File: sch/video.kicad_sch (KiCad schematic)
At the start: 4 parts

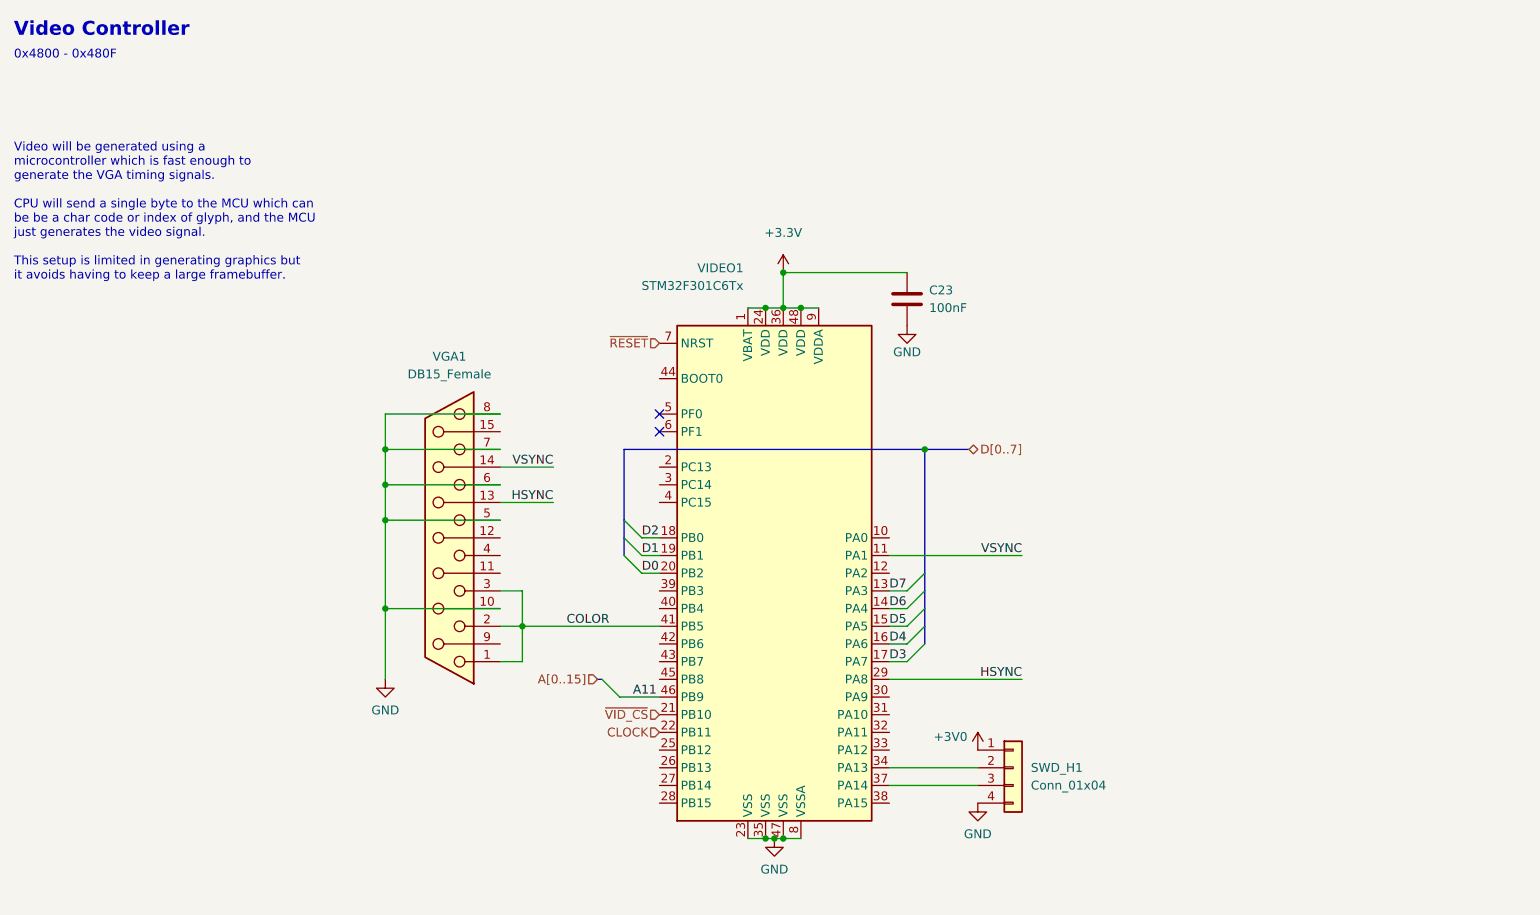
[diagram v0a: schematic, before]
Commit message: fix peripherals, add SPI
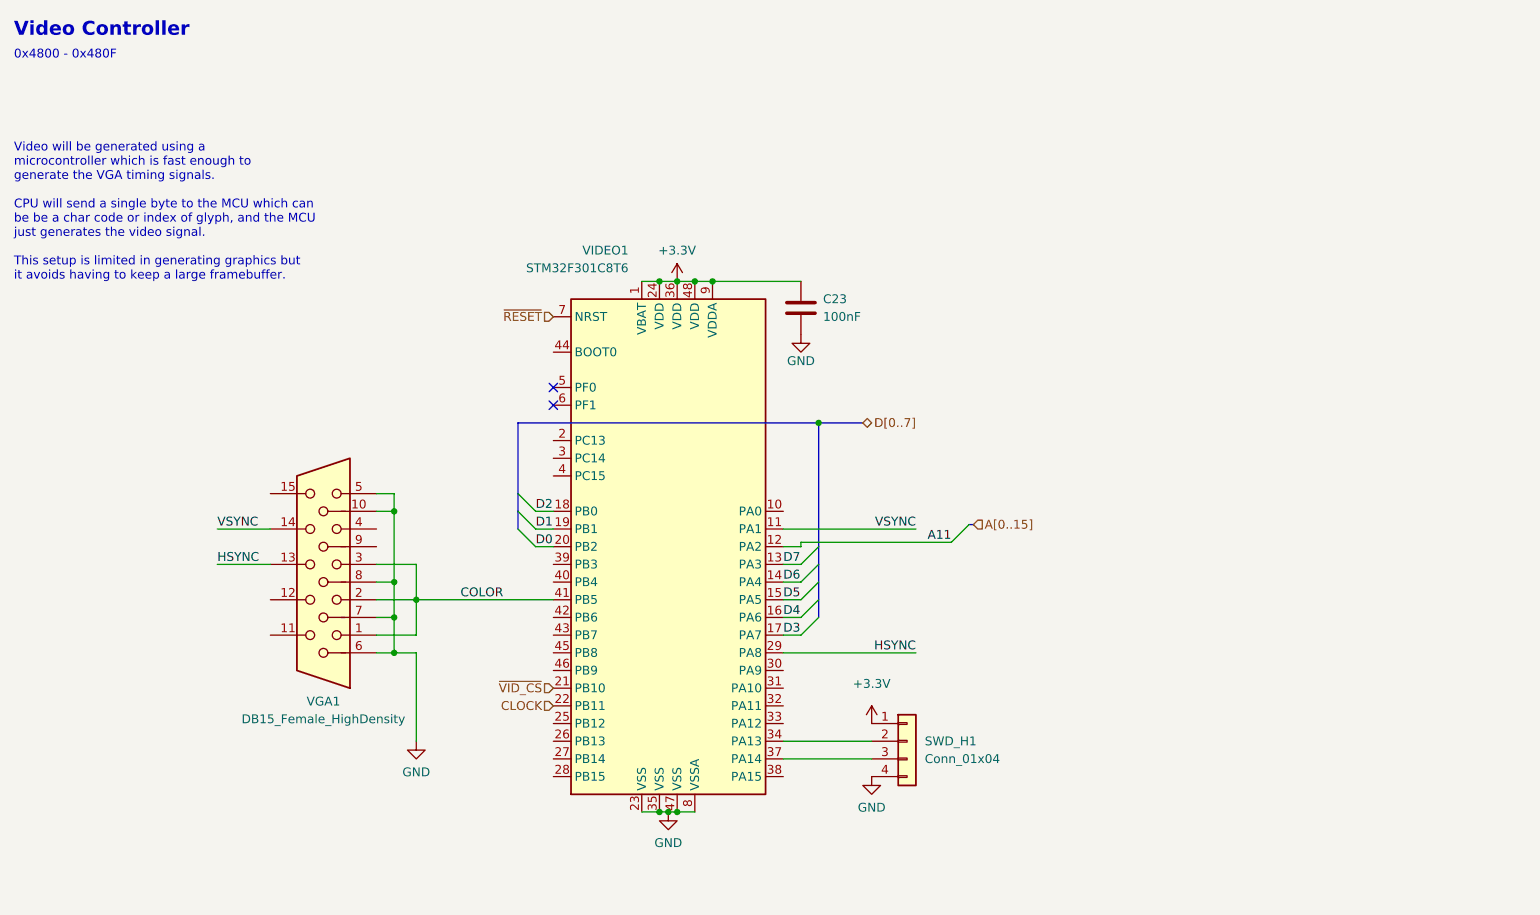
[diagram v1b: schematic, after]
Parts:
- removed VGA1: DB15_Female, Connector_Dsub:DSUB-15-HD_Female_Horizontal_P2.29x1.98mm_EdgePinOffset3.03mm_Housed_MountingHolesOffset4.94mm, symbol Connector:DB15_Female
- added VGA1: DB15_Female_HighDensity, Connector_Dsub:DSUB-15-HD_Female_Horizontal_P2.29x1.98mm_EdgePinOffset3.03mm_Housed_MountingHolesOffset4.94mm, symbol Connector:DB15_Female_HighDensity
- VIDEO1: value STM32F301C6Tx -> STM32F301C8T6; footprint Package_QFP:LQFP-48_7x7mm_P0.5mm -> Package_QFP:TQFP-48_7x7mm_P0.5mm
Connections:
- net +3V0 is gone; now on net +3V3: SWD_H1.1 (Pin_1)
- net A11: now also VIDEO1.12 (PA2); no longer VIDEO1.46 (PB9)
- net COLOR: now also VGA1.1, VGA1.2, VGA1.3
- net GND: now also VGA1.10, VGA1.5, VGA1.6, VGA1.7, VGA1.8
- net HSYNC: now also VGA1.13
- net VSYNC: now also VGA1.14
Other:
- moved on the sheet: C23, SWD_H1, VIDEO1

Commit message: Clearances
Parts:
- removed VIDEO1: STM32F301C8T6, Package_QFP:TQFP-48_7x7mm_P0.5mm, symbol MCU_ST_STM32F3:STM32F301C6Tx
- added C12: (no value), Capacitor_SMD:C_0805_2012Metric, symbol Device:C
- added C13: 100nF, Capacitor_SMD:C_0805_2012Metric, symbol Device:C
- added C14: (no value), symbol Device:C
- added R1, R3, R32, R33, R34, R35, R4: (no value), symbol Device:R
- added VIDEO1: (no value), symbol MCU_Microchip_PIC32:PIC32MX270F256D-IPT
- PROG1: renamed from SWD_H1; value Conn_01x04 -> (none); footprint Connector_PinHeader_2.00mm:PinHeader_1x04_P2.00mm_Vertical -> (none); symbol Connector_Generic:Conn_01x04 -> Connector_Generic:Conn_01x05
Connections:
- net +3V3: now also PROG1.2 (Pin_2), C13.1, R35.1, VIDEO1.17 (AVDD), VIDEO1.28 (VDD), VIDEO1.40 (VDD); no longer PROG1.1 (Pin_1)
- net A11: now also VIDEO1.44 (RB8)
- net CLOCK: now also VIDEO1.43 (RB7)
- net D0: now also VIDEO1.11 (RB13)
- net D1: now also VIDEO1.9 (RB11)
- net D2: now also VIDEO1.8 (RB10)
- net D3: now also VIDEO1.5 (RC9)
- net D4: now also VIDEO1.4 (RC8)
- net D5: now also VIDEO1.3 (RC7)
- net D6: now also VIDEO1.2 (RC6)
- net D7: now also VIDEO1.1 (RB9)
- net GND: now also PROG1.3 (Pin_3), VGA1.9, C12.2, C13.2, C14.2, VIDEO1.16 (AVSS), VIDEO1.29 (VSS), VIDEO1.39 (VSS), VIDEO1.6 (VSS); no longer PROG1.4 (Pin_4)
- net HSYNC: now also VIDEO1.19 (RA0)
- net VSYNC: now also VIDEO1.20 (RA1)
- net ~{RESET}: now also PROG1.1 (Pin_1), C14.1, R35.2, VIDEO1.18 (~{MCLR})
- net ~{VID_CS}: now also VIDEO1.15 (RB15)
- removed net COLOR: VGA1.1, VGA1.2, VGA1.3
- new net: R3.2, VIDEO1.23 (RB2)
- new net: R32.2, VIDEO1.22 (RB1)
- new net: R34.2, VIDEO1.41 (RB5)
- new net: C12.1, VIDEO1.7 (VCAP)
- new net: R1.2, VIDEO1.21 (RB0)
- new net: PROG1.5 (Pin_5), VIDEO1.12 (RA10)
- new net: PROG1.4 (Pin_4), VIDEO1.13 (RA7)
- new net: R33.2, VIDEO1.24 (RB3)
- new net: R4.2, VIDEO1.33 (RB4)
- new net BLUE: R1.1, R32.1, VGA1.3
- new net GREEN: R3.1, R33.1, VGA1.2
- new net RED: R34.1, R4.1, VGA1.1
- no-connect marks 2 -> 18
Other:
- note added: "Programming can be done with PICkit3 programmer made by Microchip. They provide an IDE called MPLAB X which take a .hex file and flashes it into memory."
- note added: "Two bits are used for each color, this gives us 6 bit color and 32 colors in theory. Ideas from this article https://blogs.fsfe.org/pboddie/?p=1712"
- moved on the sheet: C23, VGA1

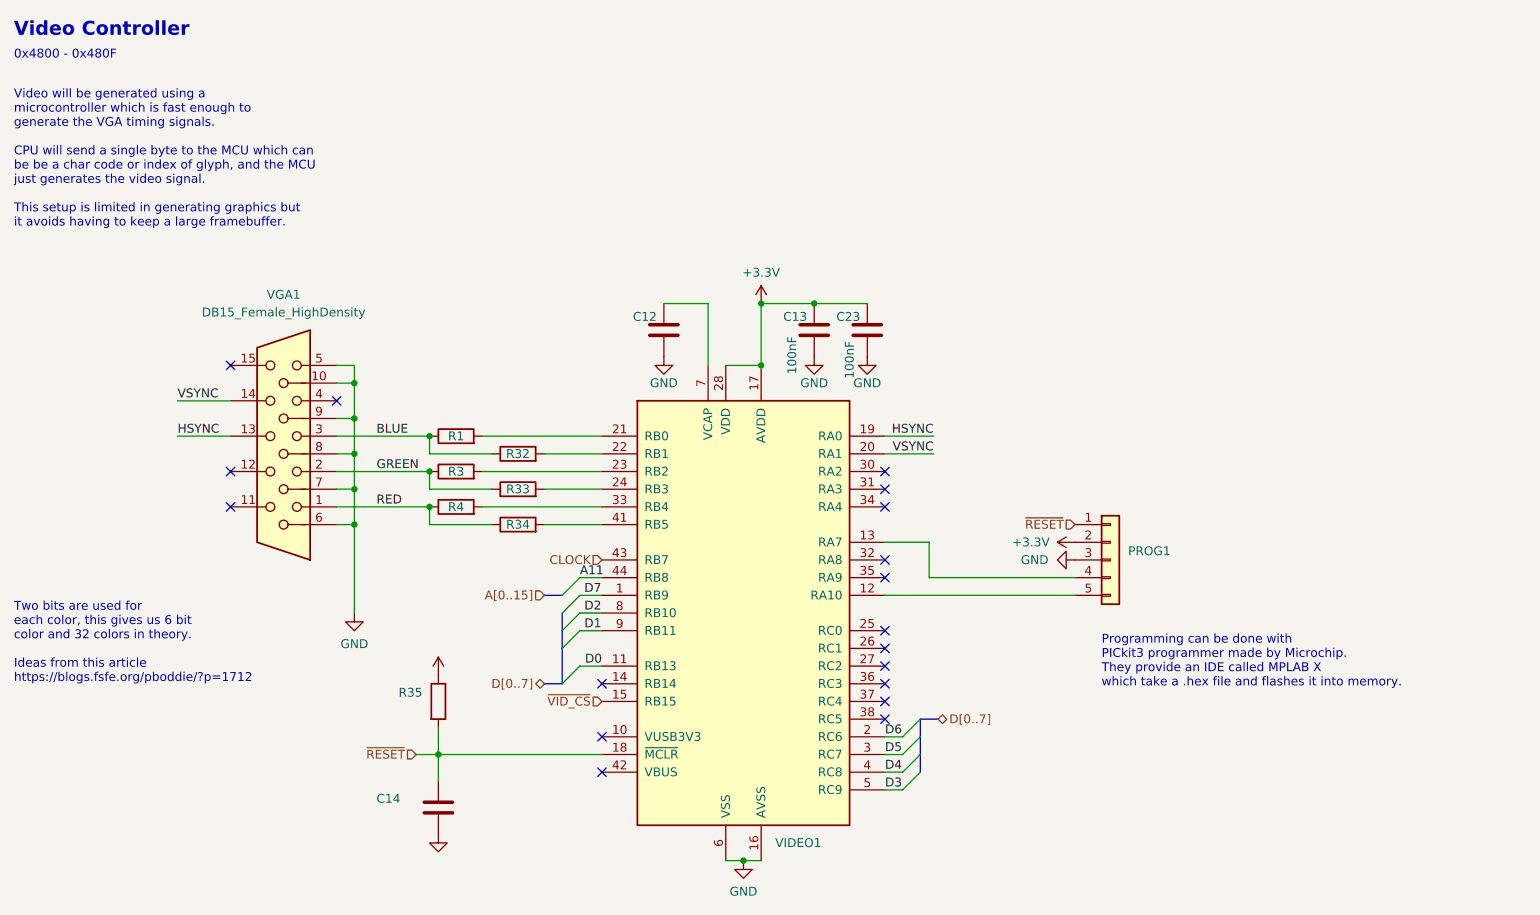
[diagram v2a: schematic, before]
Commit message: Huge mistake CPU fp
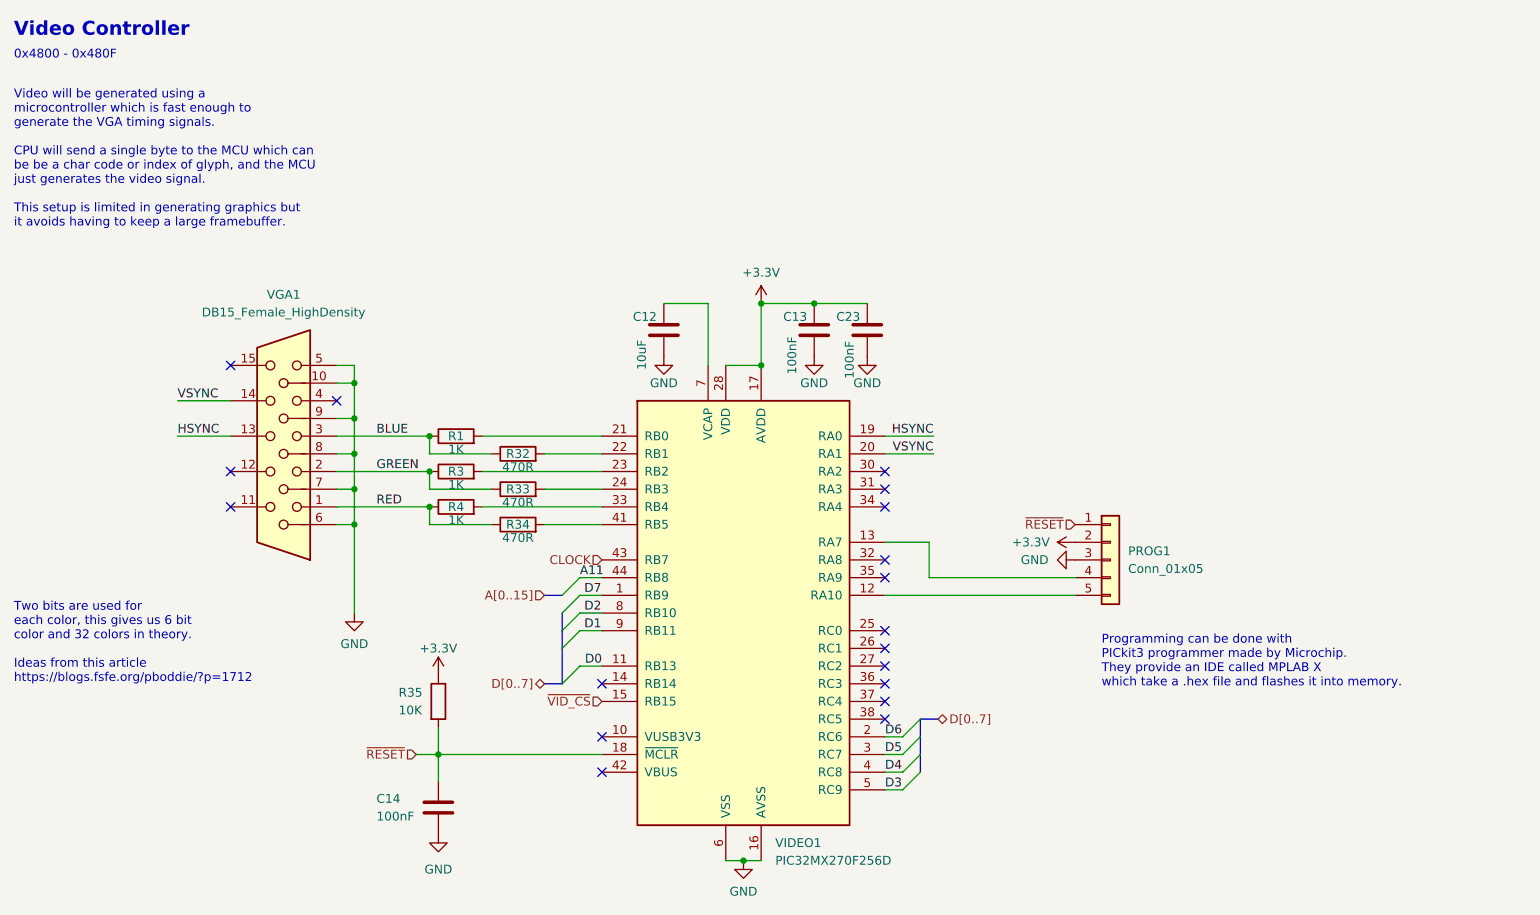
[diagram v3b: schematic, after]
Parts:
- C12: value (none) -> 10uF
- C14: value (none) -> 100nF; footprint (none) -> Capacitor_SMD:C_0805_2012Metric
- PROG1: value (none) -> Conn_01x05; footprint (none) -> Connector_PinHeader_2.00mm:PinHeader_1x05_P2.00mm_Vertical
- R1, R3, R4: value (none) -> 1K; footprint (none) -> Resistor_SMD:R_0805_2012Metric
- R32, R33, R34: value (none) -> 470R; footprint (none) -> Resistor_SMD:R_0805_2012Metric
- R35: value (none) -> 10K; footprint (none) -> Resistor_SMD:R_0805_2012Metric
- VIDEO1: value (none) -> PIC32MX270F256D; footprint (none) -> Package_QFP:TQFP-44_10x10mm_P0.8mm
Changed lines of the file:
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@@
     (in_bom yes) (on_board yes)
     (property "Reference" "R3" (id 0) (at 95.25 87.63 90))
-    (property "Value" "" (id 1) (at 95.25 89.535 90))
-    (property "Footprint" "" (id 2) (at 95.25 89.408 90)
+    (property "Value" "1K" (id 1) (at 95.25 89.535 90))
+    (property "Footprint" "Resistor_SMD:R_0805_2012Metric" (id 2) (at 95.25 89.408 90)
       (effects (font (size 1.27 1.27)) hide)
     )
@@
       (effects (font (size 1.27 1.27)) hide)
     )
-    (property "Value" "" (id 1) (at 92.71 113.03 0))
+    (property "Value" "+3.3V" (id 1) (at 92.71 113.03 0))
     (property "Footprint" "" (id 2) (at 92.71 116.84 0)
       (effects (font (size 1.27 1.27)) hide)
@@
     (in_bom yes) (on_board yes)
     (property "Reference" "R32" (id 0) (at 104.14 85.09 90))
-    (property "Value" "" (id 1) (at 104.14 86.995 90))
-    (property "Footprint" "" (id 2) (at 104.14 86.868 90)
+    (property "Value" "470R" (id 1) (at 104.14 86.995 90))
+    (property "Footprint" "Resistor_SMD:R_0805_2012Metric" (id 2) (at 104.14 86.868 90)
       (effects (font (size 1.27 1.27)) hide)
     )
@@
     (in_bom yes) (on_board yes)
     (property "Reference" "R34" (id 0) (at 104.14 95.25 90))
-    (property "Value" "" (id 1) (at 104.14 97.155 90))
-    (property "Footprint" "" (id 2) (at 104.14 97.028 90)
+    (property "Value" "470R" (id 1) (at 104.14 97.155 90))
+    (property "Footprint" "Resistor_SMD:R_0805_2012Metric" (id 2) (at 104.14 97.028 90)
       (effects (font (size 1.27 1.27)) hide)
     )
@@
       (effects (font (size 1.27 1.27)) (justify left))
     )
-    (property "Value" "" (id 1) (at 121.92 73.025 90)
+    (property "Value" "10uF" (id 1) (at 121.92 73.025 90)
       (effects (font (size 1.27 1.27)) (justify left))
     )
@@
       (effects (font (size 1.27 1.27)) hide)
     )
-    (property "Value" "" (id 1) (at 92.71 144.78 0))
+    (property "Value" "GND" (id 1) (at 92.71 144.78 0))
     (property "Footprint" "" (id 2) (at 92.71 139.7 0)
       (effects (font (size 1.27 1.27)) hide)
@@
     (in_bom yes) (on_board yes)
     (property "Reference" "R1" (id 0) (at 95.25 82.55 90))
-    (property "Value" "" (id 1) (at 95.25 84.455 90))
-    (property "Footprint" "" (id 2) (at 95.25 84.328 90)
+    (property "Value" "1K" (id 1) (at 95.25 84.455 90))
+    (property "Footprint" "Resistor_SMD:R_0805_2012Metric" (id 2) (at 95.25 84.328 90)
       (effects (font (size 1.27 1.27)) hide)
     )
@@
       (effects (font (size 1.27 1.27)) (justify left))
     )
-    (property "Value" "" (id 1) (at 141.0844 143.51 0)
-      (effects (font (size 1.27 1.27)) (justify left))
-    )
-    (property "Footprint" "" (id 2) (at 140.335 71.12 0)
+    (property "Value" "PIC32MX270F256D" (id 1) (at 141.0844 143.51 0)
+      (effects (font (size 1.27 1.27)) (justify left))
+    )
+    (property "Footprint" "Package_QFP:TQFP-44_10x10mm_P0.8mm" (id 2) (at 140.335 71.12 0)
       (effects (font (size 1.27 1.27)) (justify left) hide)
     )
@@
     (in_bom yes) (on_board yes)
     (property "Reference" "R4" (id 0) (at 95.25 92.71 90))
-    (property "Value" "" (id 1) (at 95.25 94.615 90))
-    (property "Footprint" "" (id 2) (at 95.25 94.488 90)
+    (property "Value" "1K" (id 1) (at 95.25 94.615 90))
+    (property "Footprint" "Resistor_SMD:R_0805_2012Metric" (id 2) (at 95.25 94.488 90)
       (effects (font (size 1.27 1.27)) hide)
     )
@@
       (effects (font (size 1.27 1.27)) (justify left))
     )
-    (property "Value" "" (id 1) (at 83.82 137.16 0)
-      (effects (font (size 1.27 1.27)) (justify left))
-    )
-    (property "Footprint" "" (id 2) (at 93.6752 139.7 0)
+    (property "Value" "100nF" (id 1) (at 83.82 137.16 0)
+      (effects (font (size 1.27 1.27)) (justify left))
+    )
+    (property "Footprint" "Capacitor_SMD:C_0805_2012Metric" (id 2) (at 93.6752 139.7 0)
       (effects (font (size 1.27 1.27)) hide)
     )
@@
       (effects (font (size 1.27 1.27)) (justify left))
     )
-    (property "Value" "" (id 1) (at 191.77 101.5999 0)
-      (effects (font (size 1.27 1.27)) (justify left))
-    )
-    (property "Footprint" "" (id 2) (at 189.23 100.33 0)
+    (property "Value" "Conn_01x05" (id 1) (at 191.77 101.5999 0)
+      (effects (font (size 1.27 1.27)) (justify left))
+    )
+    (property "Footprint" "Connector_PinHeader_2.00mm:PinHeader_1x05_P2.00mm_Vertical" (id 2) (at 189.23 100.33 0)
       (effects (font (size 1.27 1.27)) hide)
     )
@@
       (effects (font (size 1.27 1.27)) (justify left))
     )
-    (property "Value" "" (id 1) (at 86.995 121.92 0)
-      (effects (font (size 1.27 1.27)) (justify left))
-    )
-    (property "Footprint" "" (id 2) (at 90.932 120.65 90)
+    (property "Value" "10K" (id 1) (at 86.995 121.92 0)
+      (effects (font (size 1.27 1.27)) (justify left))
+    )
+    (property "Footprint" "Resistor_SMD:R_0805_2012Metric" (id 2) (at 90.932 120.65 90)
       (effects (font (size 1.27 1.27)) hide)
     )
@@
     (in_bom yes) (on_board yes)
     (property "Reference" "R33" (id 0) (at 104.14 90.17 90))
-    (property "Value" "" (id 1) (at 104.14 92.075 90))
-    (property "Footprint" "" (id 2) (at 104.14 91.948 90)
-      (effects (font (size 1.27 1.27)) hide)
-    )
+    (property "Value" "470R" (id 1) (at 104.14 92.075 90))
+    (property "Footprint" "Resistor_SMD:R_0805_2012Metric" (id 2) (at 104.14 91.948 90)
+      (effects (font (size 1.27 1.27)) hide)
+    )
